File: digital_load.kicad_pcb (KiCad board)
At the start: 4 copper layers, 50 x 50 mm, 71 parts, among them J1 Conn_01x02, J2 USB_C_Receptacle_USB2.0, J3 Conn_01x04, J301 Conn_PIC_ICSP_ICD, J4 Conn_01x04, Q501 IPA60R800CE, Q502 Q_NMOS_GSD, Q503 Q_NMOS_GSD, Q504 Q_NMOS_GSD, SW601 PEC11R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

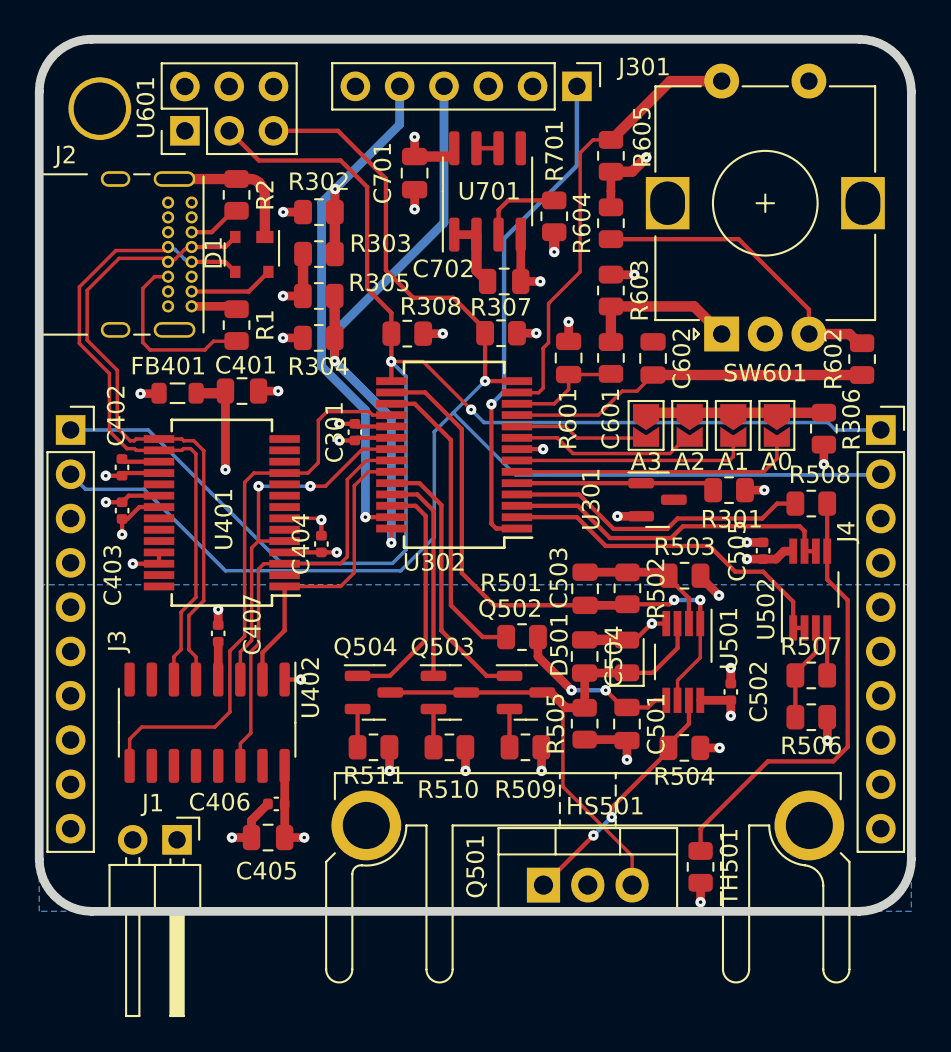
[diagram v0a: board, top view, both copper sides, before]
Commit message: Fix and tune differential pair and zones
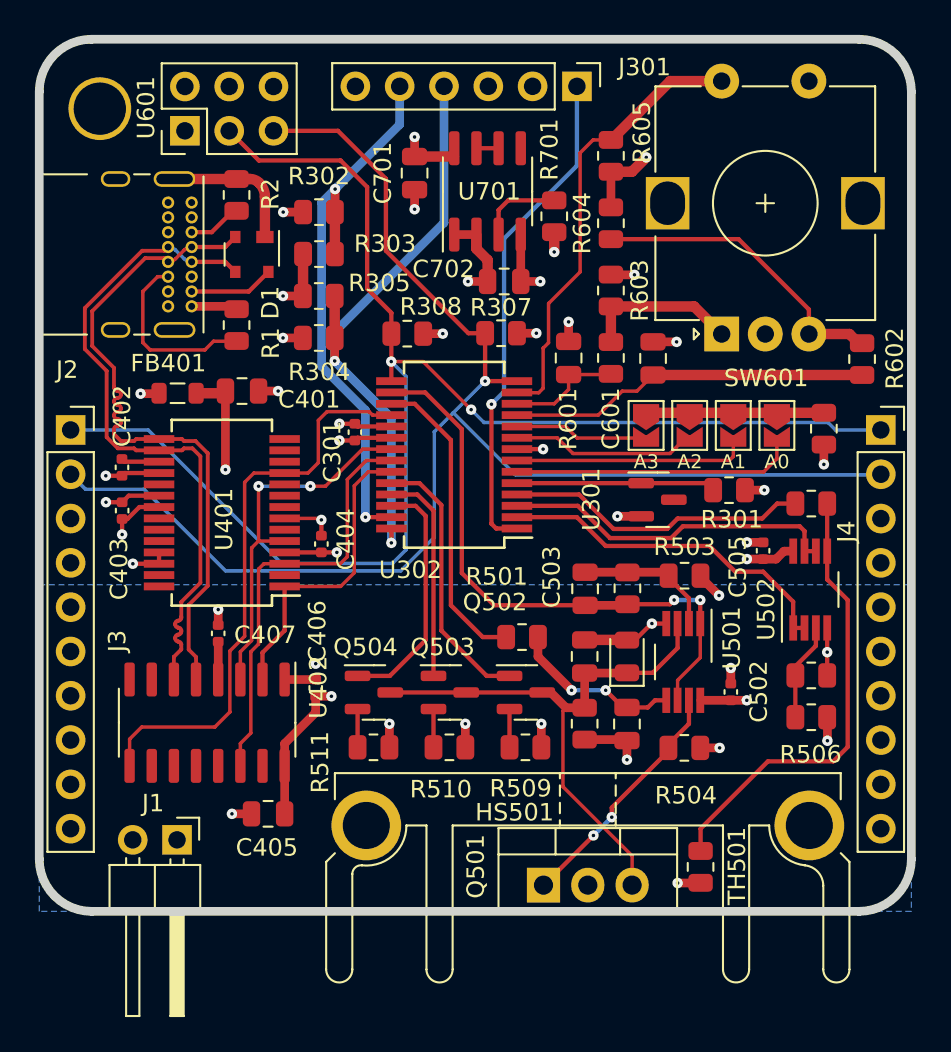
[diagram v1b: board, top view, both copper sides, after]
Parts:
- moved C406 7.03 mm to (115.8, 117.2), turned to 90 degrees
- moved C405 1.36 mm to (113.1, 124.4)
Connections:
- J3 pad 10: GND -> /Connectors/load_in
- J3 pad 5: /Connectors/load_in -> GND
- J3 pad 6: /Connectors/load_in -> GND
- J3 pad 7: /Connectors/load_in -> GND
- J3 pad 8: GND -> /Connectors/load_in
- J3 pad 9: GND -> /Connectors/load_in
- J4 pad 10: GND -> /Connectors/load_in
- J4 pad 5: /Connectors/load_in -> GND
- J4 pad 6: /Connectors/load_in -> GND
- J4 pad 7: /Connectors/load_in -> GND
- J4 pad 8: GND -> /Connectors/load_in
- J4 pad 9: GND -> /Connectors/load_in
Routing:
- net +5V: track 18.4 -> 21.5 mm
- net +3V3: track 21.6 -> 22.7 mm, vias 9 -> 10
- net /Connectors/USB2.0.D+: track 37.7 -> 38.7 mm
- net GND: track 66.3 -> 67.3 mm, vias 26 -> 28
- net /Connectors/I2C.SCL: track 84.8 -> 84.0 mm
- added copper zone on In2.Cu, net /Connectors/load_in

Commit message: Add partnumbers
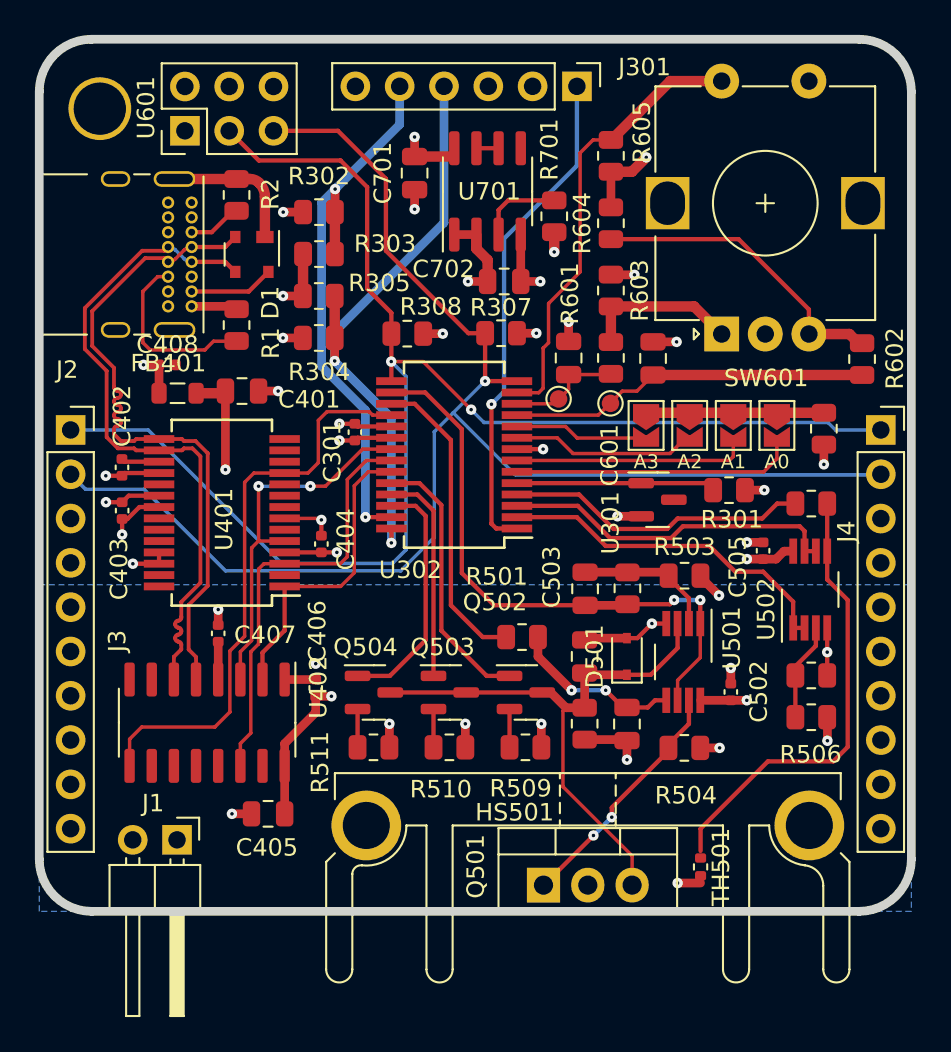
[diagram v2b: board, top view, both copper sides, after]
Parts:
- added C408: 100n, Capacitor_SMD:C_0402_1005Metric, F.Cu at (107.3, 98.7)
- added TP300: ~, TestPoint:TestPoint_Pad_D1.0mm, F.Cu at (129.8, 100.6)
- added TP301: ~, TestPoint:TestPoint_Pad_D1.0mm, F.Cu at (132.8, 100.9)
- C501: value C -> 10u
- C503: value C -> 10n
- D1: value SP0503BAHT -> SP0503BAHTG
- D501: footprint Diode_SMD:D_0805_2012Metric -> Diode_SMD:D_SOD-323
- J3, J4: value Conn_01x04 -> Conn_01x10
- R501, R503: value R_US -> 10k
- R502: value R_US -> 270k
- R508: value 50k -> 10k
- TH501: footprint Resistor_SMD:R_0805_2012Metric -> Resistor_SMD:R_0402_1005Metric
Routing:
- net +5V: track 21.5 -> 22.9 mm

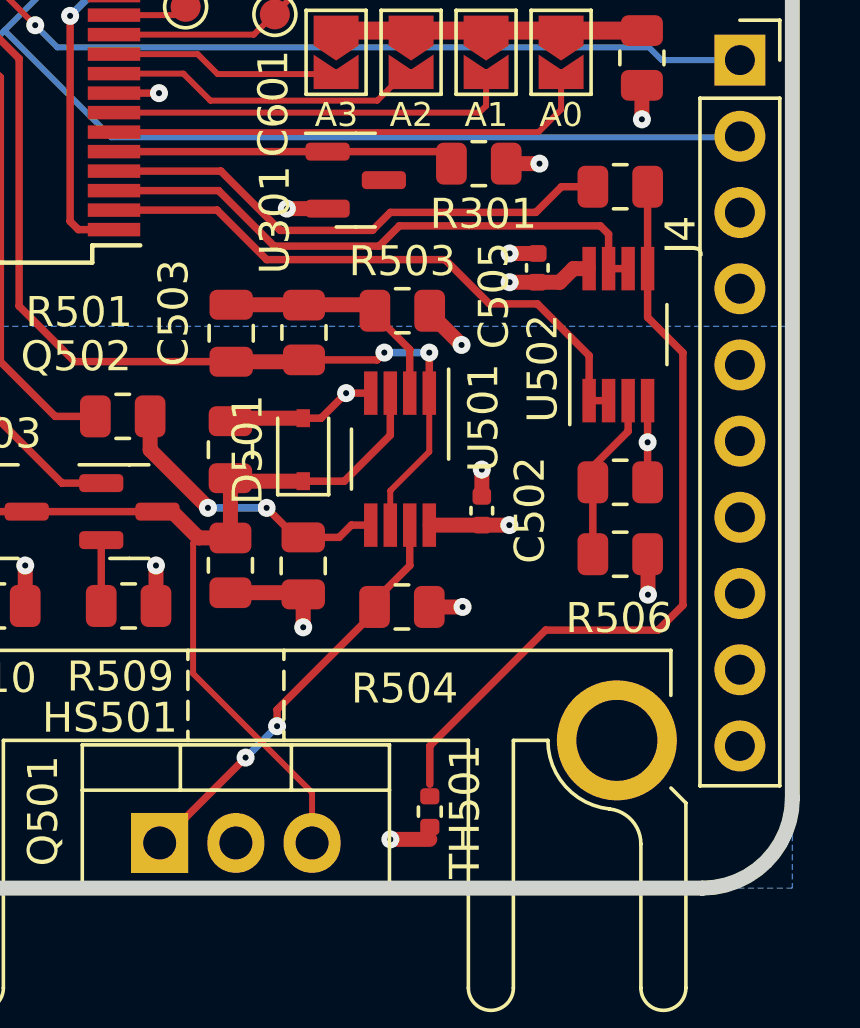
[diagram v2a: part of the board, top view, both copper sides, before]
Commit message: Fix missing footprints in schematic
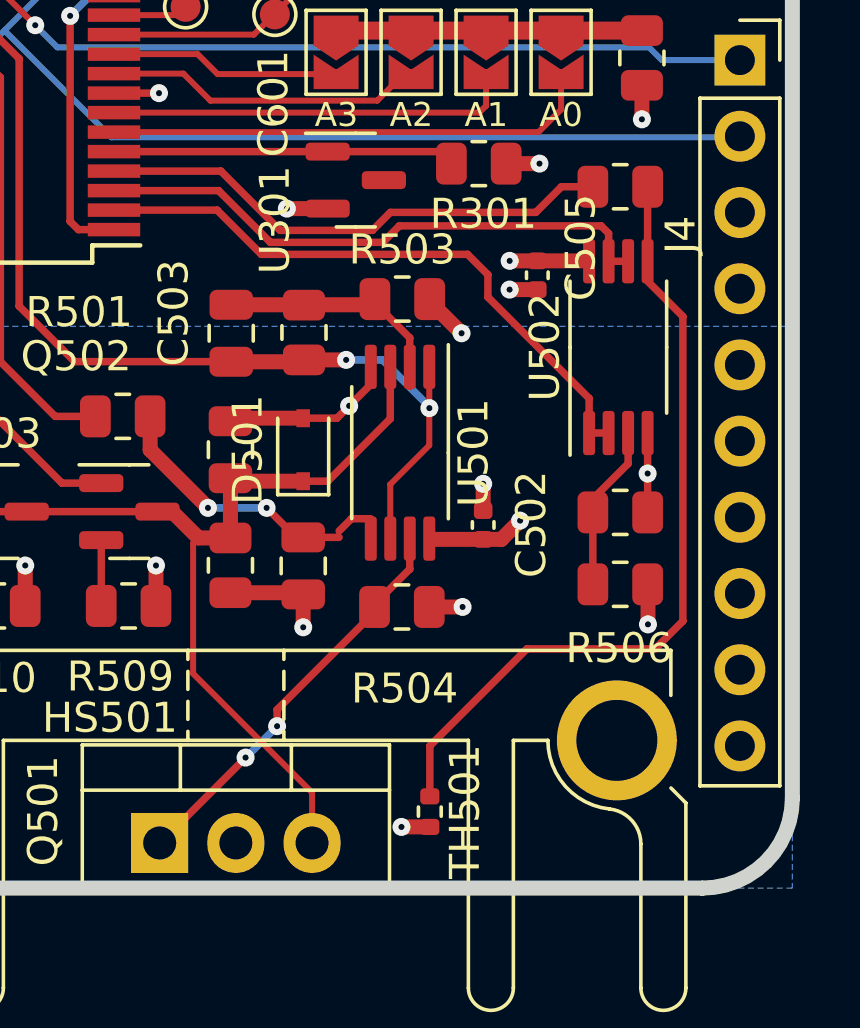
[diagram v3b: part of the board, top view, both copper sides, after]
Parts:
- C504: value C -> 10n
- U501, U502: value LM358 -> LM2904BA; footprint Package_SO:VSSOP-8_3.0x3.0mm_P0.65mm -> Package_SO:TSSOP-8_4.4x3mm_P0.65mm
- moved R506 1.00 mm to (144.3, 119.9)
- moved R507 1.00 mm to (144.3, 117.5)
- moved C502 0.48 mm to (139.7, 117.9)
- moved U502 0.42 mm to (144.2, 112.0)
- moved R503 0.39 mm to (137.0, 110.4)
- moved C505 0.25 mm to (141.5, 109.6), turned to -90 degrees
- moved U501 0.21 mm to (136.9, 115.5)
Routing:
- net +5V: track 22.9 -> 23.5 mm
- net /load_control/current_measure: track 34.0 -> 34.5 mm

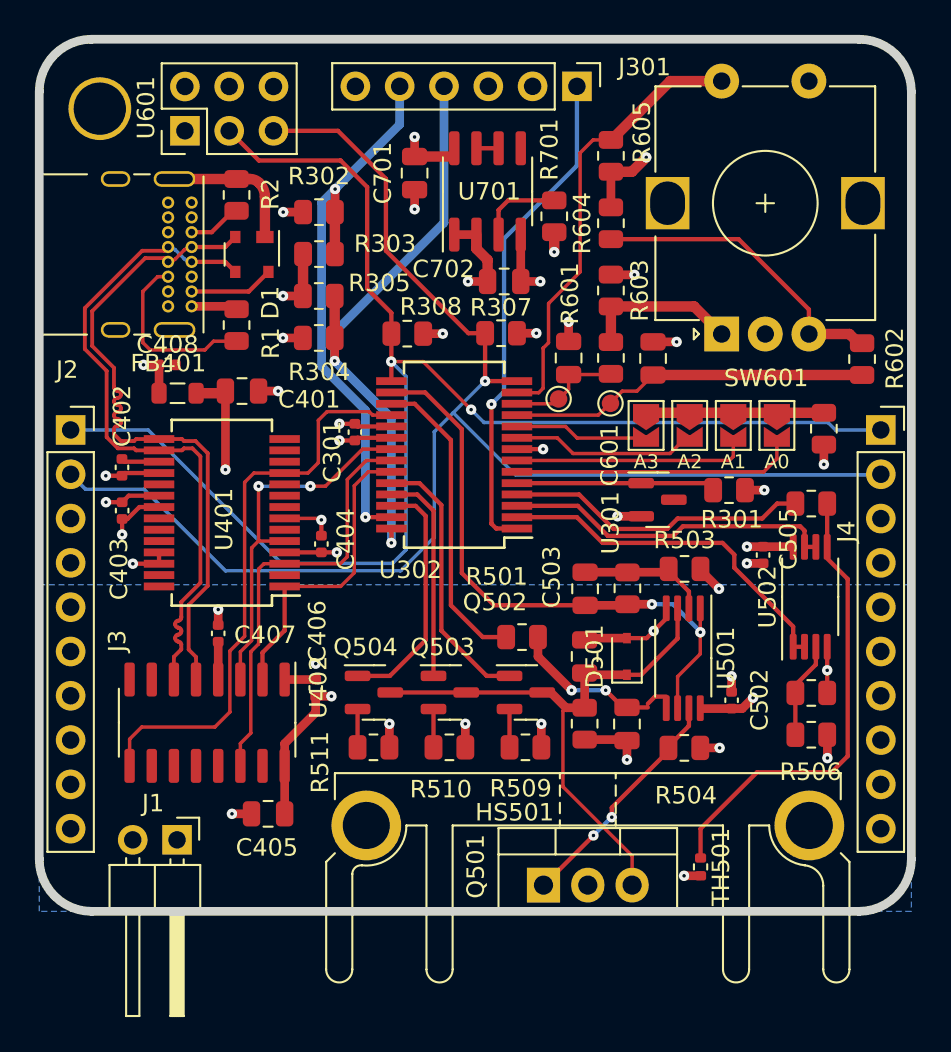
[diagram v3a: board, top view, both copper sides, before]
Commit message: Add feedback resistors for regulator
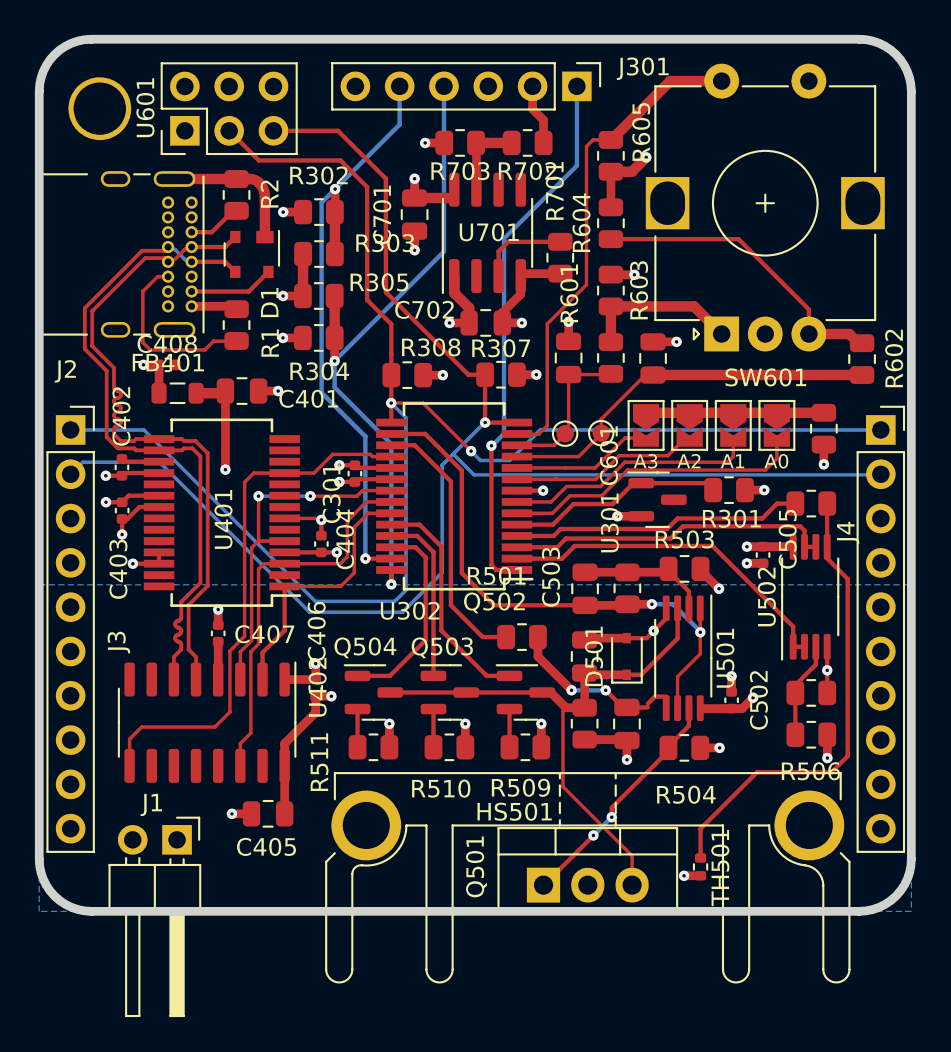
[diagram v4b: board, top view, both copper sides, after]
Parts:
- added R702: 200k, Resistor_SMD:R_0805_2012Metric, F.Cu at (128.0, 85.9)
- added R703: 120k, Resistor_SMD:R_0805_2012Metric, F.Cu at (124.1, 85.9)
- moved C702 2.60 mm to (125.6, 96.3)
- moved R701 2.40 mm to (129.9, 92.5)
- moved R307 2.38 mm to (126.5, 99.2)
- moved C301 2.38 mm to (118.1, 104.9)
- moved C701 2.38 mm to (121.5, 90.1)
- moved R308 2.38 mm to (121.1, 99.3)
- moved U302 2.38 mm to (123.8, 106.2)
- moved U701 2.38 mm to (125.7, 91.1)
- moved TP300 2.03 mm to (130.2, 102.6)
- moved TP301 1.79 mm to (132.2, 102.6)
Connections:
- U701 pad 2: +3V3 -> unconnected-(U701-Pad2)
- U701 pad 6: Net-(U701-Pad6) -> unconnected-(U701-Pad6)
- U701 pad 7: Net-(U701-Pad6) -> Net-(U701-Pad7)
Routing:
- net Net-(U701-Pad7): track 0.00 -> 4.73 mm
- net /Connectors/I2C.SDA: track 84.5 -> 88.1 mm
- net /Connectors/I2C.SCL: track 84.0 -> 87.0 mm
- net GND: track 67.5 -> 70.2 mm
- net /microcontroller/UART.RTS: track 33.0 -> 30.6 mm
- net /microcontroller/~{MCLR}/VPP: track 28.7 -> 31.1 mm
- net /load_control/range.100ma: track 12.3 -> 9.89 mm
- net /Display_Encoder/select: track 25.8 -> 28.2 mm
- net /microcontroller/UART.RX: track 17.6 -> 15.2 mm
- net /load_control/pwm_ctrl: track 17.7 -> 15.3 mm
- net /Display_Encoder/ENC.A: track 6.60 -> 8.97 mm
- net /microcontroller/5V_sense: track 34.8 -> 37.1 mm
- net /microcontroller/3V3_sense: track 32.8 -> 35.2 mm
- net /load_control/range.1ma: track 15.6 -> 13.2 mm
- net /load_control/range.10a: track 14.1 -> 11.7 mm
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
